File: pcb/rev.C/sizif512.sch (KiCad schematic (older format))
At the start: 186 parts, among them J1 DS-210, J10 RCJ-014, J11 PinHeader, J12 PJ-313, J13 PinHeader, J14 PinHeader, J15 PJ-313, J16 MEM2055-00-190-01-A, J17 PinHeader, J2 Conn_02x28_Row_Letter_First, J3 PinHeader, J4 DS1020-08, J5 DS1020-05, J6 PinHeader, J7 DB9-M, J8 PinHeader, J9 Mini-DIN-9, Q1 BC547C, Q2 BC547C, Q3 BC547C, Q4 BC547C, SW1 Jumper, SW2 Button THT, SW3 Button THT, U1 LM2596T-ADJ, U10 SN74CB3T3245PW, U11 AD724, U12 AS6C4008-55PCN, U13 74HCT4053D, U14 AY-3-8910, U15 LM311N, U2 AMS1117-3.3, U3 SN74CB3T3245PW, U4 Z84C0010PEC, U5 SN74CB3T3245PW, U6 EPM1270T144, U7 SN74CB3T3245PW, U8 SST39SF040, U9 74HCU04, Y1 28 MHz, Y2 4.433 MHz

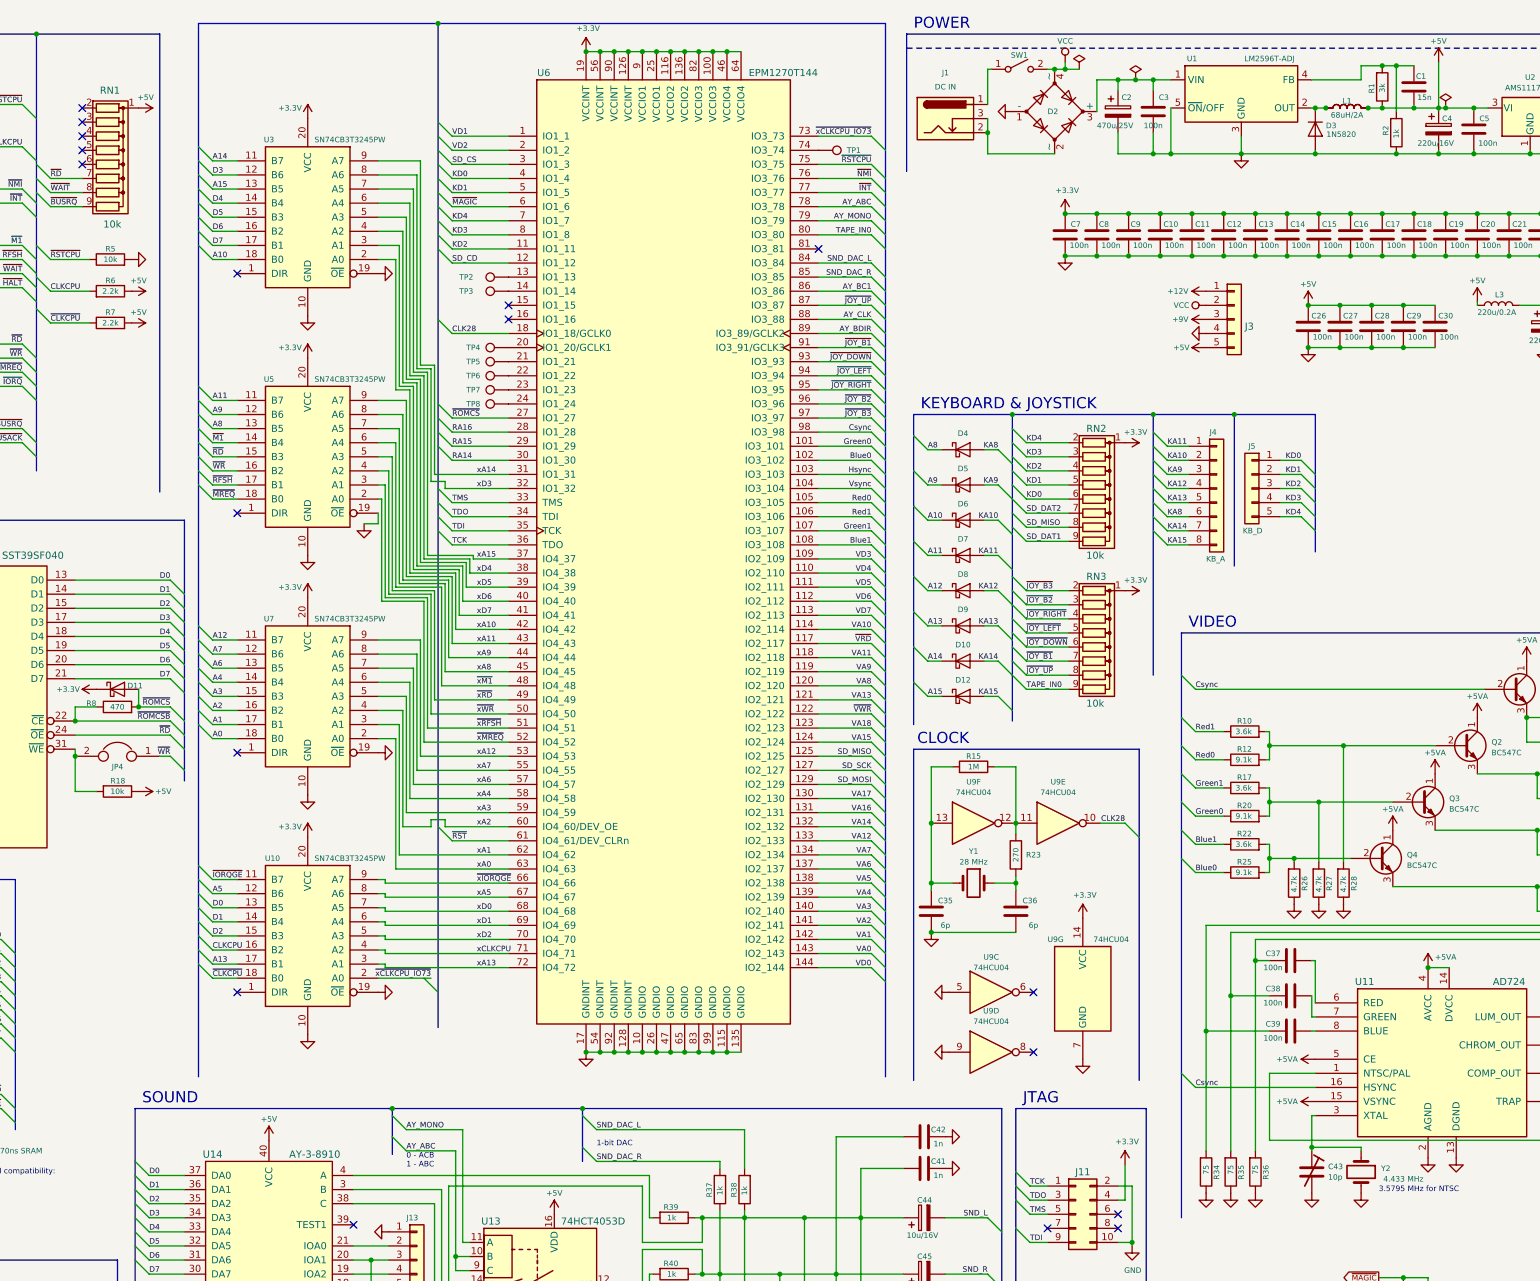
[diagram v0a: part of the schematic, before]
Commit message: pcb rev.C: minor layout changes
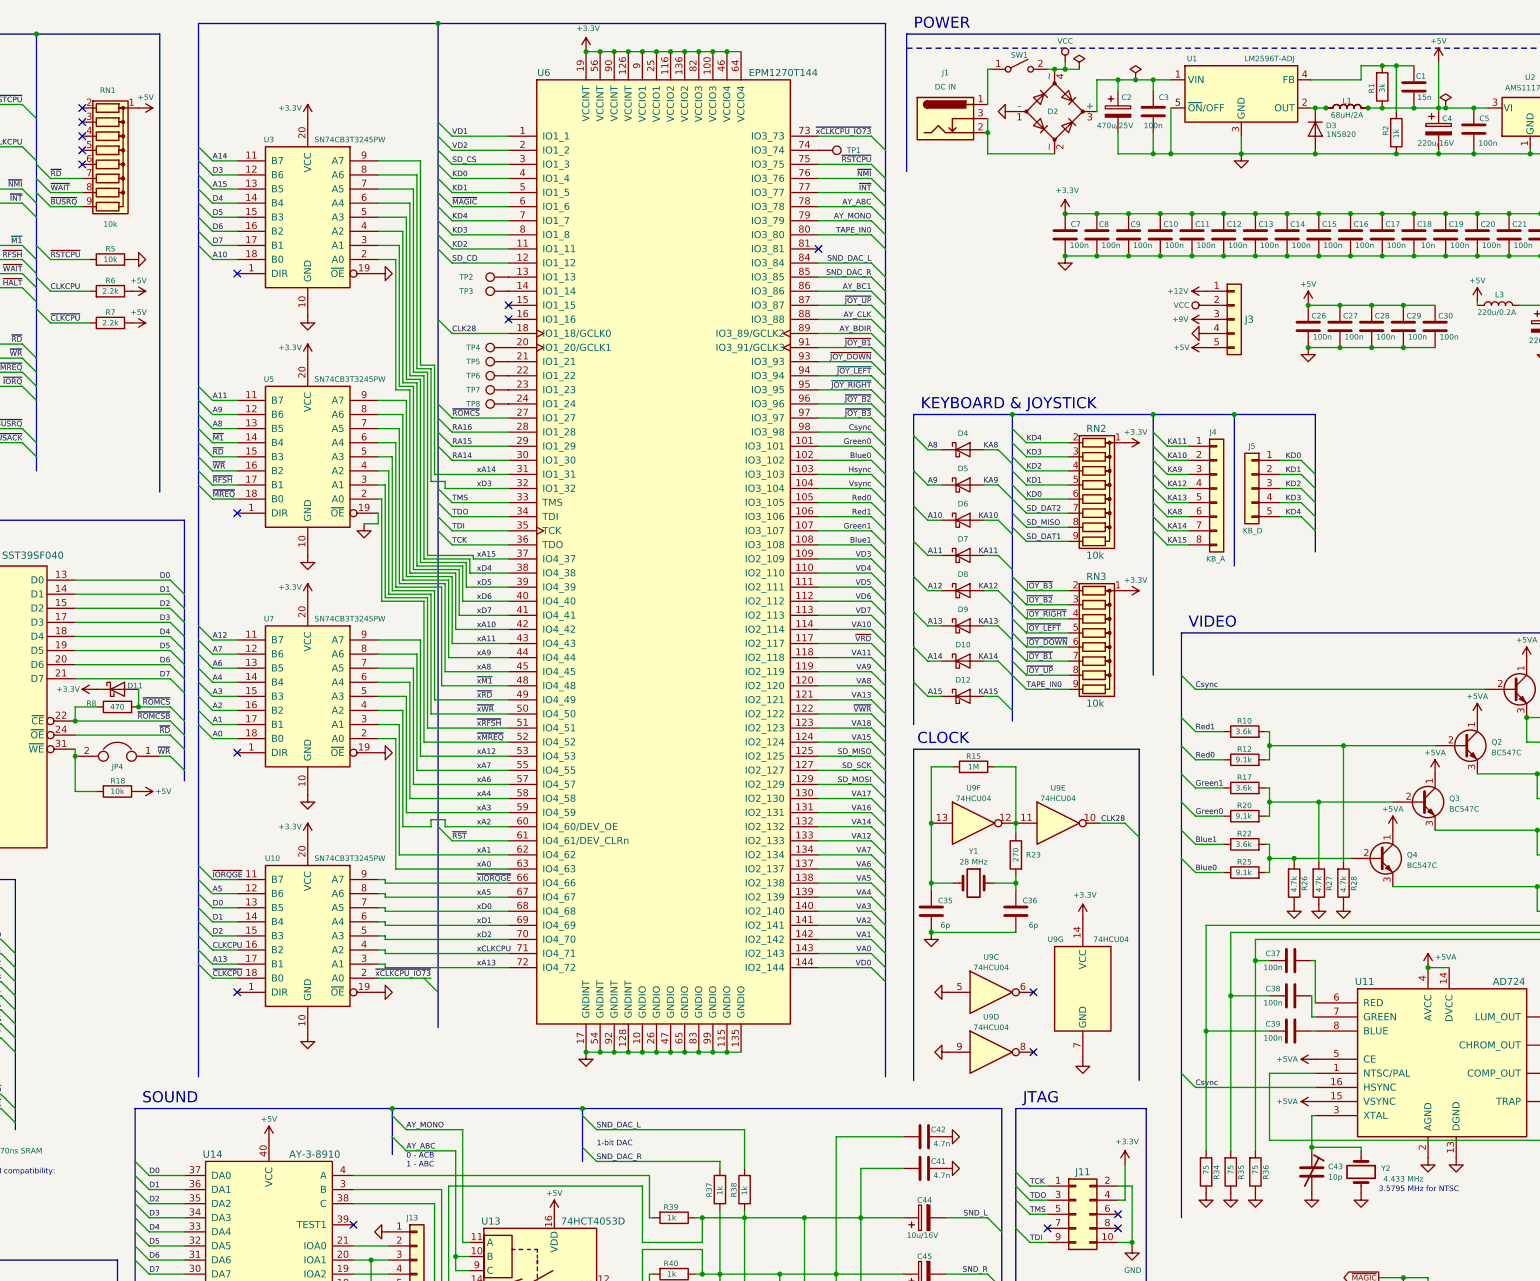
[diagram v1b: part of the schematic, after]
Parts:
- C18: value 100n -> 10n
- C41, C42: value 1n -> 4.7n
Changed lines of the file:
@@
 	0    1    1    0
 $EndComp
-$Comp
-L Device:R_Network08 RN1
-U 1 1 612FF54F
-P 3100 1575
-F 0 "RN1" V 2575 1500 50  0000 L CNN
-F 1 "10k" V 3525 1525 50  0000 L CNN
-F 2 "Resistor_THT:R_Array_SIP9" V 3575 1575 50  0001 C CNN
-F 3 "http://www.vishay.com/docs/31509/csc.pdf" H 3100 1575 50  0001 C CNN
-	1    3100 1575
-	0    1    1    0
-$EndComp
 Text Label 2675 1875 0    39   ~ 0
 ~BUSRQ
@@
 U 4 1 5D9B4031
 P 9350 7875
-F 0 "U9" H 9350 8168 39  0000 C CNN
-F 1 "74HCU04" H 9350 8093 39  0000 C CNN
+F 0 "U9" H 9350 8125 39  0000 C CNN
+F 1 "74HCU04" H 9350 8050 39  0000 C CNN
 F 2 "Package_DIP:DIP-14_W7.62mm_Socket" H 9350 7875 50  0001 C CNN
 F 3 "https://assets.nexperia.com/documents/data-sheet/74HC_HCT04.pdf" H 9350 7875 50  0001 C CNN
@@
 U 6 1 5CFBEB43
 P 9225 6250
-F 0 "U9" H 9225 6543 39  0000 C CNN
-F 1 "74HCU04" H 9225 6468 39  0000 C CNN
+F 0 "U9" H 9225 6500 39  0000 C CNN
+F 1 "74HCU04" H 9225 6425 39  0000 C CNN
 F 2 "Package_DIP:DIP-14_W7.62mm_Socket" H 9225 6250 50  0001 C CNN
 F 3 "https://assets.nexperia.com/documents/data-sheet/74HC_HCT04.pdf" H 9225 6250 50  0001 C CNN
@@
 U 5 1 5D9B7FD5
 P 9825 6250
-F 0 "U9" H 9825 6543 39  0000 C CNN
-F 1 "74HCU04" H 9825 6468 39  0000 C CNN
+F 0 "U9" H 9825 6500 39  0000 C CNN
+F 1 "74HCU04" H 9825 6425 39  0000 C CNN
 F 2 "Package_DIP:DIP-14_W7.62mm_Socket" H 9825 6250 50  0001 C CNN
 F 3 "https://assets.nexperia.com/documents/data-sheet/74HC_HCT04.pdf" H 9825 6250 50  0001 C CNN
@@
 	12225 875  12350 875
 Wire Wire Line
-	11650 1500 11125 1500
-Wire Wire Line
 	12225 1200 12225 875
 $Comp
@@
 $EndComp
 $Comp
-L Device:CP C31
-U 1 1 5EDD4449
-P 13275 2725
-F 0 "C31" H 13400 2800 39  0000 R CNN
-F 1 "220u/16V" H 13425 2625 39  0000 R CNN
-F 2 "Capacitor_THT:CP_Radial_D8.0mm_P3.50mm" H 13313 2575 50  0001 C CNN
-F 3 "~" H 13275 2725 50  0001 C CNN
-	1    13275 2725
-	1    0    0    -1
-$EndComp
-$Comp
 L Device:C C32
 U 1 1 5EDD5A80
@@
 P 8875 8475
 F 0 "C42" V 8925 8375 39  0000 C CNN
-F 1 "1n" V 8825 8375 39  0000 C CNN
+F 1 "4.7n" V 8825 8350 39  0000 C CNN
 F 2 "Capacitor_THT:C_Disc_D5.0mm_W2.5mm_P2.50mm" H 8913 8325 50  0001 C CNN
 F 3 "~" H 8875 8475 50  0001 C CNN
@@
 P 8875 8700
 F 0 "C41" V 8925 8600 39  0000 C CNN
-F 1 "1n" V 8825 8600 39  0000 C CNN
+F 1 "4.7n" V 8825 8575 39  0000 C CNN
 F 2 "Capacitor_THT:C_Disc_D5.0mm_W2.5mm_P2.50mm" H 8913 8550 50  0001 C CNN
 F 3 "~" H 8875 8700 50  0001 C CNN
@@
 U 1 1 6720E1D9
 P 11075 2675
-F 0 "J3" H 11150 2625 50  0000 L CNN
+F 0 "J3" H 11150 2675 50  0000 L CNN
 F 1 "PinHeader" H 11155 2576 50  0001 L CNN
 F 2 "Connector_PinHeader_2.54mm:PinHeader_1x05_P2.54mm_Vertical" H 11075 2675 50  0001 C CNN
@@
 $EndComp
 $Comp
-L Device:C C8
-U 1 1 5E4A403B
-P 10100 2075
-F 0 "C8" H 10050 2150 39  0000 C CNN
-F 1 "100n" H 10000 2000 39  0000 C CNN
-F 2 "Capacitor_SMD:C_0805_2012Metric_Pad1.15x1.40mm_HandSolder" H 10138 1925 50  0001 C CNN
-F 3 "~" H 10100 2075 50  0001 C CNN
-	1    10100 2075
-	-1   0    0    -1
-$EndComp
-$Comp
 L Device:C C18
 U 1 1 6128C12A
 P 12350 2075
 F 0 "C18" H 12275 2150 39  0000 C CNN
-F 1 "100n" H 12250 2000 39  0000 C CNN
+F 1 "10n" H 12250 2000 39  0000 C CNN
 F 2 "Capacitor_SMD:C_0805_2012Metric_Pad1.15x1.40mm_HandSolder" H 12388 1925 50  0001 C CNN
 F 3 "~" H 12350 2075 50  0001 C CNN
@@
 $EndComp
 Connection ~ 10100 1925
-$Comp
-L Device:C C7
-U 1 1 6292270F
-P 9875 2075
-F 0 "C7" H 9800 2000 39  0000 C CNN
-F 1 "100n" H 9775 2150 39  0000 C CNN
-F 2 "Capacitor_THT:C_Disc_D5.0mm_W2.5mm_P2.50mm" H 9913 1925 50  0001 C CNN
-F 3 "~" H 9875 2075 50  0001 C CNN
-	1    9875 2075
-	-1   0    0    1
-$EndComp
 Wire Wire Line
 	9875 1925 10100 1925
@@
 Wire Bus Line
 	8600 575  8600 8050
+Wire Wire Line
+	11125 1500 11650 1500
+$Comp
+L Device:R_Network08 RN1
+U 1 1 612FF54F
+P 3100 1575
+F 0 "RN1" V 2575 1500 39  0000 L CNN
+F 1 "10k" V 3525 1525 39  0000 L CNN
+F 2 "Resistor_THT:R_Array_SIP9" V 3575 1575 50  0001 C CNN
+F 3 "http://www.vishay.com/docs/31509/csc.pdf" H 3100 1575 50  0001 C CNN
+	1    3100 1575
+	0    1    1    0
+$EndComp
+$Comp
+L Device:CP C31
+U 1 1 5EDD4449
+P 13275 2725
+F 0 "C31" H 13400 2800 39  0000 R CNN
+F 1 "220u/16V" H 13425 2625 39  0000 R CNN
+F 2 "Capacitor_THT:CP_Radial_D8.0mm_P3.50mm" H 13313 2575 50  0001 C CNN
+F 3 "~" H 13275 2725 50  0001 C CNN
+	1    13275 2725
+	1    0    0    -1
+$EndComp
+$Comp
+L Device:C C8
+U 1 1 5E4A403B
+P 10100 2075
+F 0 "C8" H 10050 2150 39  0000 C CNN
+F 1 "100n" H 10000 2000 39  0000 C CNN
+F 2 "Capacitor_SMD:C_0805_2012Metric_Pad1.15x1.40mm_HandSolder" H 10138 1925 50  0001 C CNN
+F 3 "~" H 10100 2075 50  0001 C CNN
+	1    10100 2075
+	-1   0    0    -1
+$EndComp
+$Comp
+L Device:C C7
+U 1 1 6292270F
+P 9875 2075
+F 0 "C7" H 9800 2000 39  0000 C CNN
+F 1 "100n" H 9775 2150 39  0000 C CNN
+F 2 "Capacitor_THT:C_Disc_D5.0mm_W2.5mm_P2.50mm" H 9913 1925 50  0001 C CNN
+F 3 "~" H 9875 2075 50  0001 C CNN
+	1    9875 2075
+	-1   0    0    1
+$EndComp
 $EndSCHEMATC
